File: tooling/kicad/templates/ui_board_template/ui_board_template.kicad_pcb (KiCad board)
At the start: 2 copper layers, 39 x 26 mm, 4 parts, among them J1 Conn_01x20_Socket

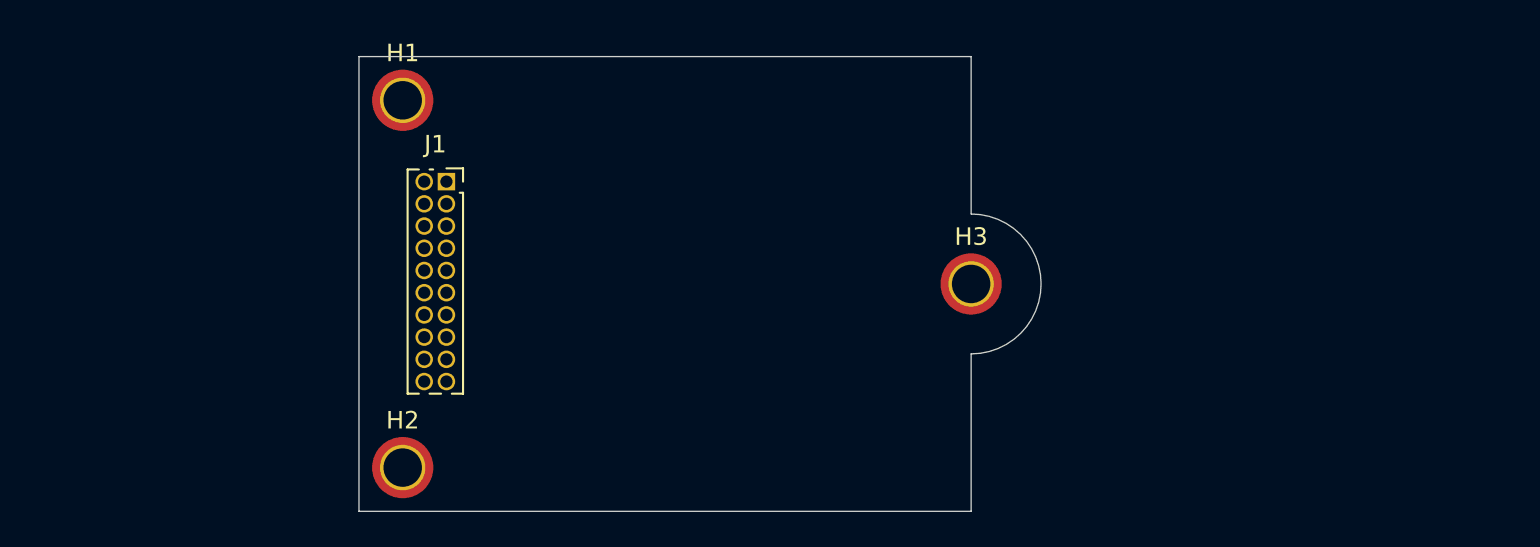
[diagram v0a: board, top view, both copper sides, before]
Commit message: [UPDATE] ui_board connector position
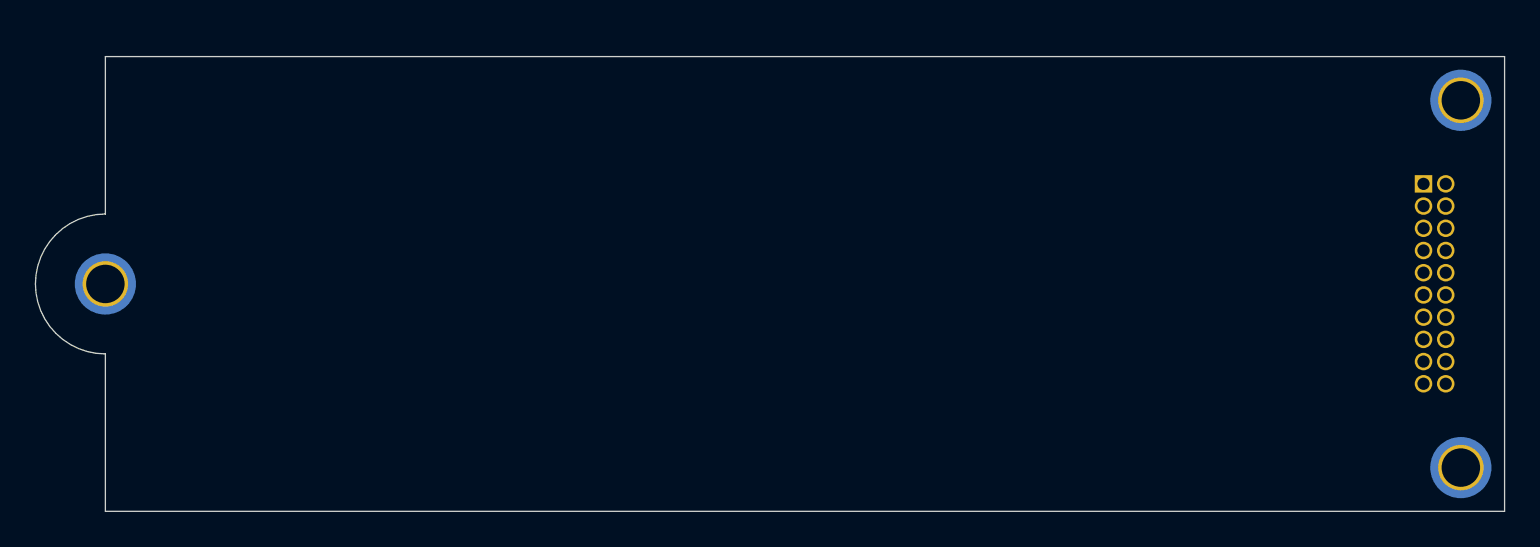
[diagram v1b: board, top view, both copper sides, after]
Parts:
- H1, H2, H3, J1: moved to B.Cu
- moved H1 64.0 mm to (163.0, 110.5)
- moved H2 64.0 mm to (163.0, 89.5)
- moved J1 56.8 mm to (161.5, 100.0), turned to 180 degrees
- moved H3 49.5 mm to (85.5, 100.0)
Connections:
- J1 pad 10: unconnected-(J1-Pin_10-Pad10) -> Net-(D3-K)
- J1 pad 11: unconnected-(J1-Pin_11-Pad11) -> Net-(D2-K)
- J1 pad 12: unconnected-(J1-Pin_12-Pad12) -> Net-(D1-K)
- J1 pad 13: unconnected-(J1-Pin_13-Pad13) -> Net-(D9-K)
- J1 pad 14: unconnected-(J1-Pin_14-Pad14) -> Net-(D10-K)
- J1 pad 15: unconnected-(J1-Pin_15-Pad15) -> Net-(D11-K)
- J1 pad 16: unconnected-(J1-Pin_16-Pad16) -> Net-(D12-K)
- J1 pad 17: unconnected-(J1-Pin_17-Pad17) -> Net-(D13-K)
- J1 pad 18: unconnected-(J1-Pin_18-Pad18) -> Net-(D14-K)
- J1 pad 19: unconnected-(J1-Pin_19-Pad19) -> Net-(D15-K)
- J1 pad 20: unconnected-(J1-Pin_20-Pad20) -> Net-(D16-K)
- J1 pad 5: unconnected-(J1-Pin_5-Pad5) -> Net-(D8-K)
- J1 pad 6: unconnected-(J1-Pin_6-Pad6) -> Net-(D7-K)
- J1 pad 7: unconnected-(J1-Pin_7-Pad7) -> Net-(D6-K)
- J1 pad 8: unconnected-(J1-Pin_8-Pad8) -> Net-(D5-K)
- J1 pad 9: unconnected-(J1-Pin_9-Pad9) -> Net-(D4-K)
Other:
- board size 39 x 26 mm -> 84 x 26 mm
